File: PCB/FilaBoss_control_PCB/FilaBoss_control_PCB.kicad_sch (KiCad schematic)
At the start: 3 parts, among them J1 Screw_Terminal_01x02

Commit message: pcb
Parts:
- removed C1: C, symbol Device:C
- added C2: C, symbol Device:C
- added F1: Fuse, symbol Device:Fuse
- added J2, J4: Screw_Terminal_01x02, symbol Connector:Screw_Terminal_01x02
- added J3: Screw_Terminal_01x04, symbol Connector:Screw_Terminal_01x04
- added J5: Barrel_Jack_PTH_Slot, PCM_SparkFun-Connector:Barrel_Jack_PTH_Slot, symbol PCM_SparkFun-Connector:Barrel_Jack_PTH_Slot
- added M1, M2: Motor_DC, symbol Motor:Motor_DC
- added Q1, Q2: Q_NMOS, Package_TO_SOT_THT:TO-220F-3_Vertical, symbol Device:Q_NMOS
- added R1, R4: 100R, Resistor_THT:R_Axial_DIN0411_L9.9mm_D3.6mm_P12.70mm_Horizontal, symbol Device:R
- added R2, R3: 10K, Resistor_THT:R_Axial_DIN0411_L9.9mm_D3.6mm_P12.70mm_Horizontal, symbol Device:R
- added U1: ESP32_C3_super_mini, custom:ESP32-super-mini, symbol custom:ESP32_C3_super_mini
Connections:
- net at L1.1: now also F1.2
- net at L1.2: now also C2.1
- new net: Q2.G, R1.1, R2.1
- new net: J4.2 (Pin_2), M1.2 (-), Q1.D
- new net: Q1.G, R3.1, R4.1
- new net: C2.2, J2.1 (Pin_1), J4.1 (Pin_1), M1.1 (+), M2.1 (+)
- new net: J2.2 (Pin_2), M2.2 (-), Q2.D
- new net +24V: F1.1
- new net GND: Q1.S, Q2.S, R2.2, R3.2, U1.12 (GND)
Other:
- moved on the sheet: L1

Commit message: pcb v1 ready
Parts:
- removed J1, J4: Screw_Terminal_01x02, symbol Connector:Screw_Terminal_01x02
- removed J3: Screw_Terminal_01x04, symbol Connector:Screw_Terminal_01x04
- removed Q1: Q_NMOS, Package_TO_SOT_THT:TO-220F-3_Vertical, symbol Device:Q_NMOS
- added A1: Pololu_Breakout_A4988, Module:Pololu_Breakout-16_15.2x20.3mm, symbol Driver_Motor:Pololu_Breakout_A4988
- added C1, C3: C, Capacitor_THT:C_Axial_L5.1mm_D3.1mm_P10.00mm_Horizontal, symbol Device:C
- added D1, D2: D, Diode_THT:D_A-405_P10.16mm_Horizontal, symbol Device:D
- added J1, J9: Conn_01x04_Encoder, PCM_SparkFun-Connector:JST_1x04_P2.0mm_Vertical_PTH, symbol PCM_SparkFun-Connector:Conn_01x04_JST_P2.0mm_Vertical_PTH
- added J3: Screw_Terminal_01x02, TerminalBlock:TerminalBlock_Xinya_XY308-2.54-2P_1x02_P2.54mm_Horizontal, symbol Connector:Screw_Terminal_01x02
- added J6: PinHeader_01x06_P2.54mm_Vertical_THT_D1mm, PCM_fab:PinHeader_01x06_P2.54mm_Vertical_THT_D1mm, symbol PCM_fab:PinHeader_01x06_P2.54mm_Vertical_THT_D1mm
- added J7: Conn_01x04, PCM_SparkFun-Connector:JST_1x04_P2.0mm_Vertical_PTH, symbol PCM_SparkFun-Connector:Conn_01x04_JST_P2.0mm_Vertical_PTH
- added J8: JST_2mm_3, PCM_SparkFun-Connector:JST_1x03_P2.0mm_Vertical_PTH, symbol PCM_SparkFun-Connector:Conn_01x03_JST_P2.0mm_Vertical_PTH
- added Q1: IRLZ44N, Package_TO_SOT_THT:TO-220-3_Vertical, symbol Transistor_FET:IRLZ44N
- added SW1: RotaryEncoder_Switch, symbol Device:RotaryEncoder_Switch
- added U2: LM78M05_TO220, Package_TO_SOT_THT:TO-220-3_Vertical, symbol Regulator_Linear:LM78M05_TO220
- C2: footprint (none) -> Capacitor_THT:C_Axial_L5.1mm_D3.1mm_P10.00mm_Horizontal
- F1: footprint (none) -> Fuse:Fuseholder_Clip-5x20mm_Keystone_3512P_Inline_P23.62x7.27mm_D1.02x2.41x1.02x1.57mm_Horizontal
- J2: footprint (none) -> TerminalBlock:TerminalBlock_Xinya_XY308-2.54-2P_1x02_P2.54mm_Horizontal
- L1: footprint (none) -> Inductor_THT_Wurth:L_Wurth_WE-HCFT-2012_LeadDiameter1.2mm; Current (none) -> 4.5A; PROD_ID (none) -> NDUC-17223
- Q2: value Q_NMOS -> IRLZ44N; footprint Package_TO_SOT_THT:TO-220F-3_Vertical -> Package_TO_SOT_THT:TO-220-3_Vertical; symbol Device:Q_NMOS -> Transistor_FET:IRLZ44N
- R1, R2, R3, R4: footprint Resistor_THT:R_Axial_DIN0411_L9.9mm_D3.6mm_P12.70mm_Horizontal -> Resistor_THT:R_Axial_DIN0207_L6.3mm_D2.5mm_P10.16mm_Horizontal
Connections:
- net +24V: now also C2.1, L1.2, M1.1 (+), A1.8 (VMOT), D2.1 (K), J3.2 (Pin_2), J6.6 (Pin_6), U2.1 (VI); no longer F1.1
- net GND: now also C2.2, J5.GND, Q2.3 (S), A1.1 (GND), A1.7 (GND), A1.9 (~{ENABLE}), C1.2, C3.2, J1.4 (Pin_4), J6.2 (Pin_2), J8.1, J9.4 (Pin_4), Q1.3 (S), SW1.C, SW1.S2, U2.2 (GND); no longer Q2.S
- net at R1.1, R2.1: now also Q2.1 (G); no longer Q2.G
- net at M1.2 (-): now also D2.2 (A), J3.1 (Pin_1), Q1.2 (D)
- net at R3.1, R4.1: now also Q1.1 (G)
- net VDC: now reaches F1.2, L1.1
- net LINE: now reaches J5.PWR
- net LINE: now also F1.1
- net at R4.2: now also U1.4 (D2/A2)
- net at R1.2: now also U1.5 (D3/A3)
- net at U1.0 (ADC1-0): now also A1.16 (DIR)
- net at U1.1 (ADC1-1): now also A1.15 (STEP)
- net at U1.10 (D10/MOSI): now also J9.3 (Pin_3), SW1.B
- net +3.3V: now reaches U1.11 (3V3)
- net +3.3V: now also A1.10 (MS1), A1.11 (MS2), A1.12 (MS3), A1.13 (~{RESET}), A1.14 (~{SLEEP}), A1.2 (VDD), J1.3 (Pin_3), J6.1 (Pin_1)
- net +5V: now reaches U1.13 (5V)
- net +5V: now also C1.1, C3.1, U2.3 (VO)
- net at U1.2 (D0/A0): now also J1.2 (Pin_2)
- net at U1.20 (D7/RX): now also J8.2
- net at U1.21 (D6/TX): now also J8.3
- net at U1.3 (D1/A1): now also J1.1 (Pin_1)
- net at U1.6 (D4/SDA): now also J6.4 (Pin_4)
- net at U1.7 (D5/SCL): now also J6.3 (Pin_3)
- net at U1.8 (D8/SCK): now also J9.1 (Pin_1), SW1.S1
- net at U1.9 (D9/MISO): now also J9.2 (Pin_2), SW1.A
- new net: D1.1 (K), J2.2 (Pin_2), J6.5 (Pin_5), M2.1 (+)
- new net: D1.2 (A), J2.1 (Pin_1), M2.2 (-), Q2.2 (D)
- new net: A1.3 (1B), J7.1 (Pin_1)
- new net: A1.4 (1A), J7.2 (Pin_2)
- new net: A1.5 (2A), J7.3 (Pin_3)
- new net: A1.6 (2B), J7.4 (Pin_4)
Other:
- moved on the sheet: C2, F1, J2, J5, L1, M2, R1, R2, U1

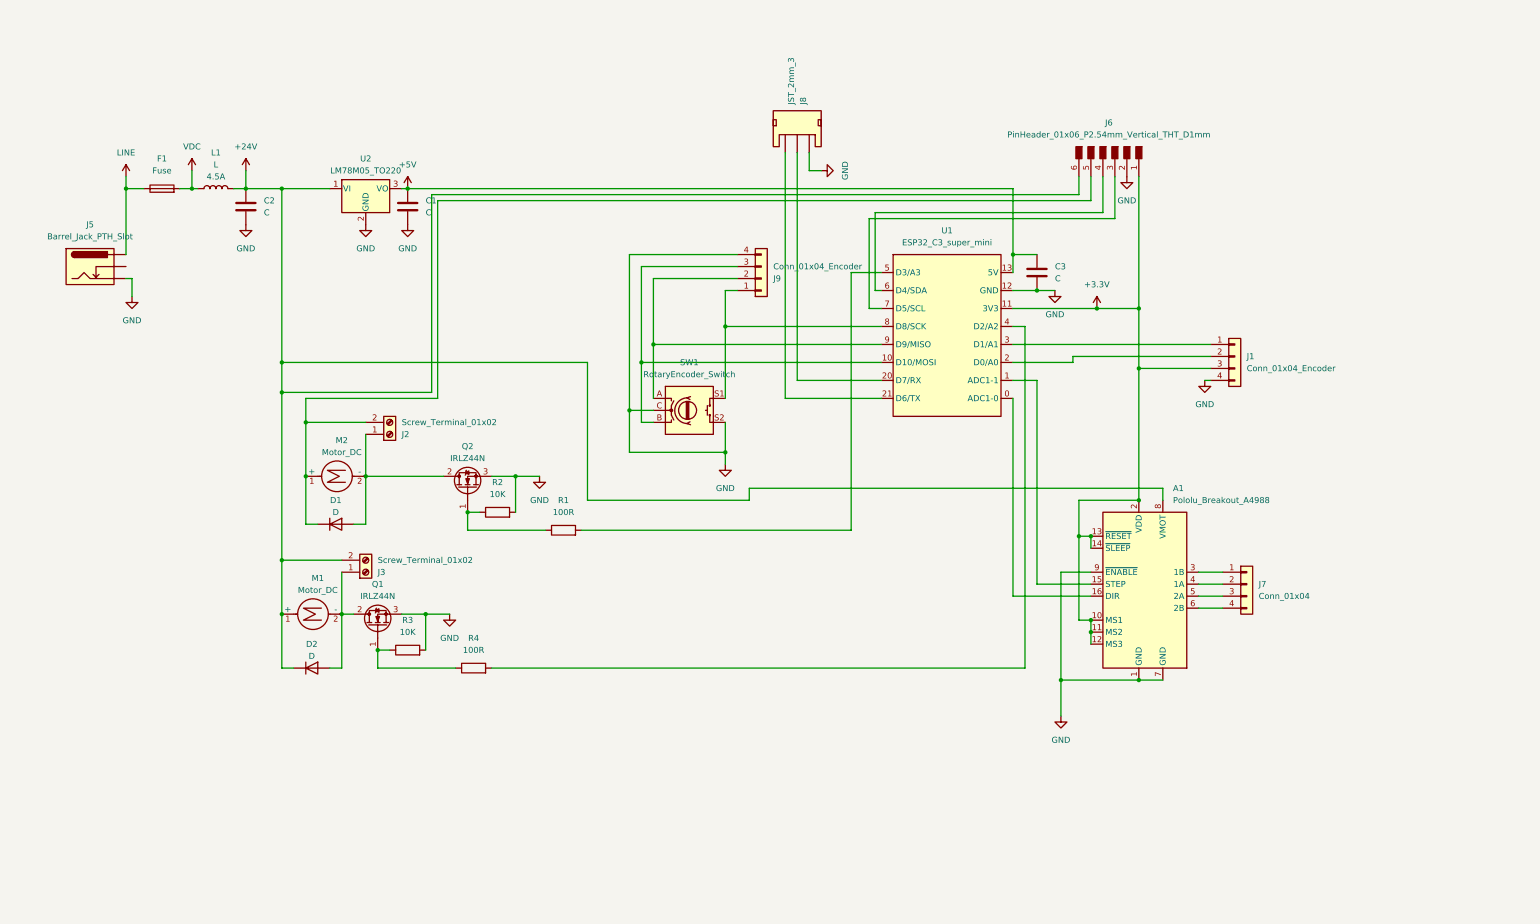
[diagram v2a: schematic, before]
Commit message: bigger esp required
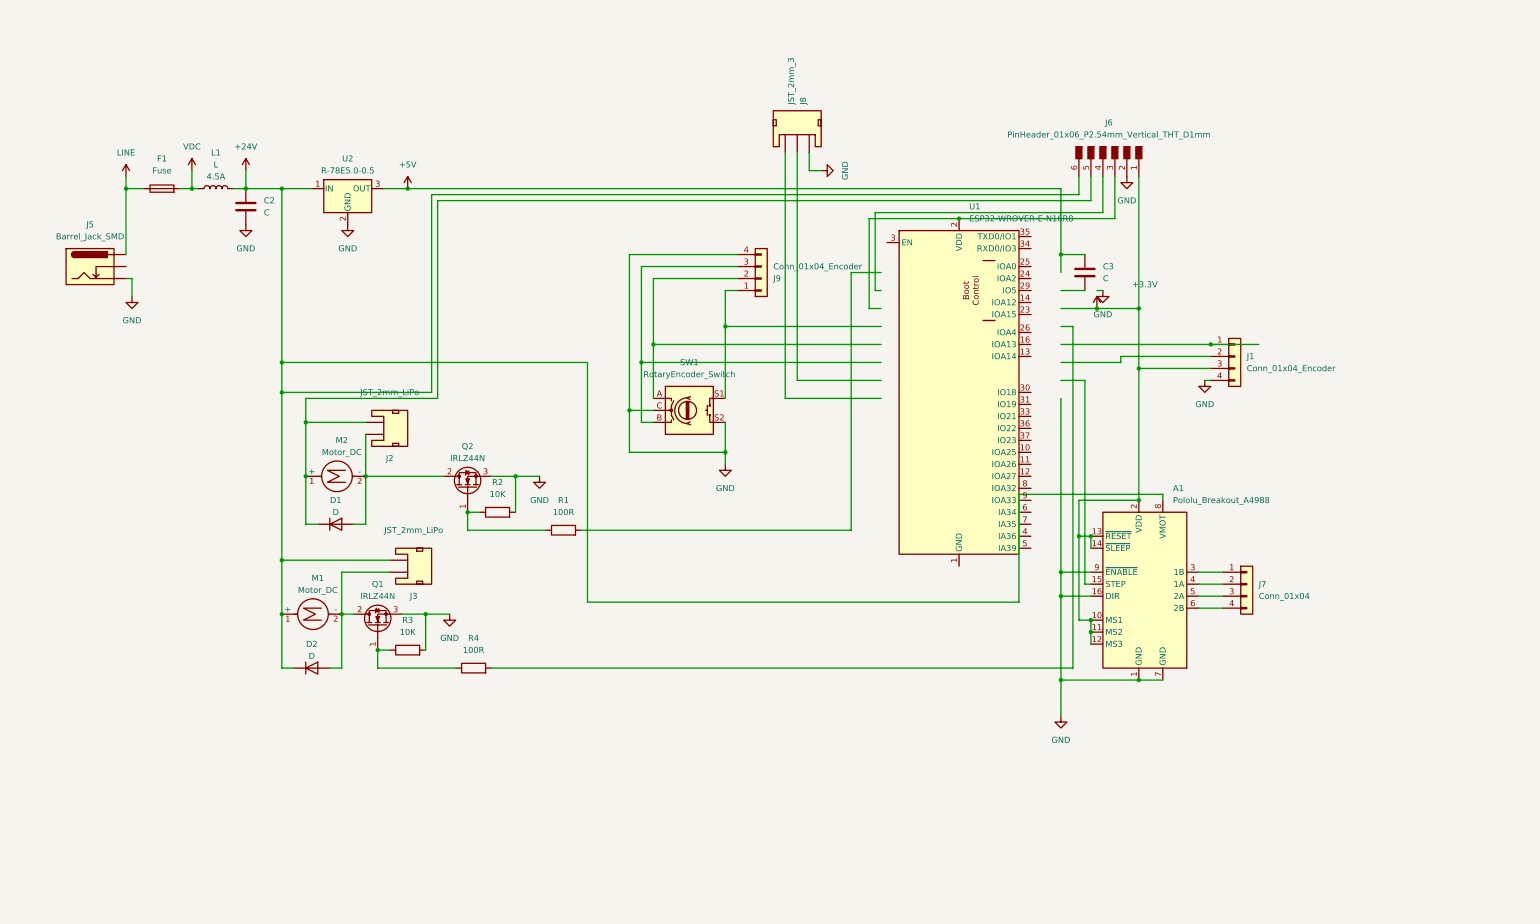
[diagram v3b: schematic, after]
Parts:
- removed C1: C, Capacitor_THT:C_Axial_L5.1mm_D3.1mm_P10.00mm_Horizontal, symbol Device:C
- removed J2, J3: Screw_Terminal_01x02, TerminalBlock:TerminalBlock_Xinya_XY308-2.54-2P_1x02_P2.54mm_Horizontal, symbol Connector:Screw_Terminal_01x02
- added J2, J3: JST_2mm_LiPo, Connector_JST:JST_PH_B2B-PH-K_1x02_P2.00mm_Vertical, symbol PCM_SparkFun-Connector:Conn_01x02_JST_P2.0mm_Horizontal_SMD
- F1: footprint Fuse:Fuseholder_Clip-5x20mm_Keystone_3512P_Inline_P23.62x7.27mm_D1.02x2.41x1.02x1.57mm_Horizontal -> Fuse:Fuseholder_Clip-5x20mm_Bel_FC-203-22_Lateral_P17.80x5.00mm_D1.17mm_Horizontal
- J5: value Barrel_Jack_PTH_Slot -> Barrel_Jack_SMD; footprint PCM_SparkFun-Connector:Barrel_Jack_PTH_Slot -> PCM_SparkFun-Connector:Barrel_Jack_SMD; symbol PCM_SparkFun-Connector:Barrel_Jack_PTH_Slot -> PCM_SparkFun-Connector:Barrel_Jack_SMD; PROD_ID CONN-08197 -> CONN-08106
- U1: value ESP32_C3_super_mini -> ESP32-WROVER-E-N16R8; footprint custom:ESP32-super-mini -> PCM_SparkFun-RF:ESP32-WROVER-E-IE; symbol custom:ESP32_C3_super_mini -> PCM_SparkFun-RF:ESP32-WROVER-E-N16R8; PROD_ID (none) -> IC-21314
- U2: value LM78M05_TO220 -> R-78E5.0-0.5; footprint Package_TO_SOT_THT:TO-220-3_Vertical -> Converter_DCDC:Converter_DCDC_RECOM_R-78E-0.5_THT; symbol Regulator_Linear:LM78M05_TO220 -> Converter_DCDC:R-78E5.0-0.5
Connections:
- net +24V: now also J3.1 (-)
- net +3.3V: no longer U1.11 (3V3)
- net +5V: no longer U1.13 (5V)
- net GND: now also A1.16 (DIR); no longer C3.2, U1.12 (GND)
- net at D2.2 (A), M1.2 (-), Q1.2 (D): now also J3.2 (+)
- net at D1.1 (K), J6.5 (Pin_5), M2.1 (+): now also J2.1 (-)
- net at D1.2 (A), M2.2 (-), Q2.2 (D): now also J2.2 (+)
- net at J9.1 (Pin_1), SW1.S1: no longer U1.8 (D8/SCK)
- net at J9.2 (Pin_2), SW1.A: no longer U1.9 (D9/MISO)
- net at J9.3 (Pin_3), SW1.B: no longer U1.10 (D10/MOSI)
- net at A1.15 (STEP): no longer U1.1 (ADC1-1)
- net at J1.1 (Pin_1): no longer U1.3 (D1/A1)
- net at J1.2 (Pin_2): no longer U1.2 (D0/A0)
- net at R4.2: no longer U1.4 (D2/A2)
- net at J6.3 (Pin_3): now also U1.2 (VDD); no longer U1.7 (D5/SCL)
- net at J6.4 (Pin_4): no longer U1.6 (D4/SDA)
- net at J8.2: no longer U1.20 (D7/RX)
- net at J8.3: no longer U1.21 (D6/TX)
- net at R1.2: no longer U1.5 (D3/A3)
- new net: U1.1 (GND), U1.15 (GND), U1.38 (GND), U1.39.1 (GND), U1.39.2 (GND), U1.39.3 (GND), U1.39.4 (GND), U1.39.5 (GND), U1.39.6 (GND), U1.39.7 (GND), U1.39.8 (GND), U1.39.9 (GND)
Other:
- moved on the sheet: C3, U2

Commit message: pcb converted to esp32 wroom
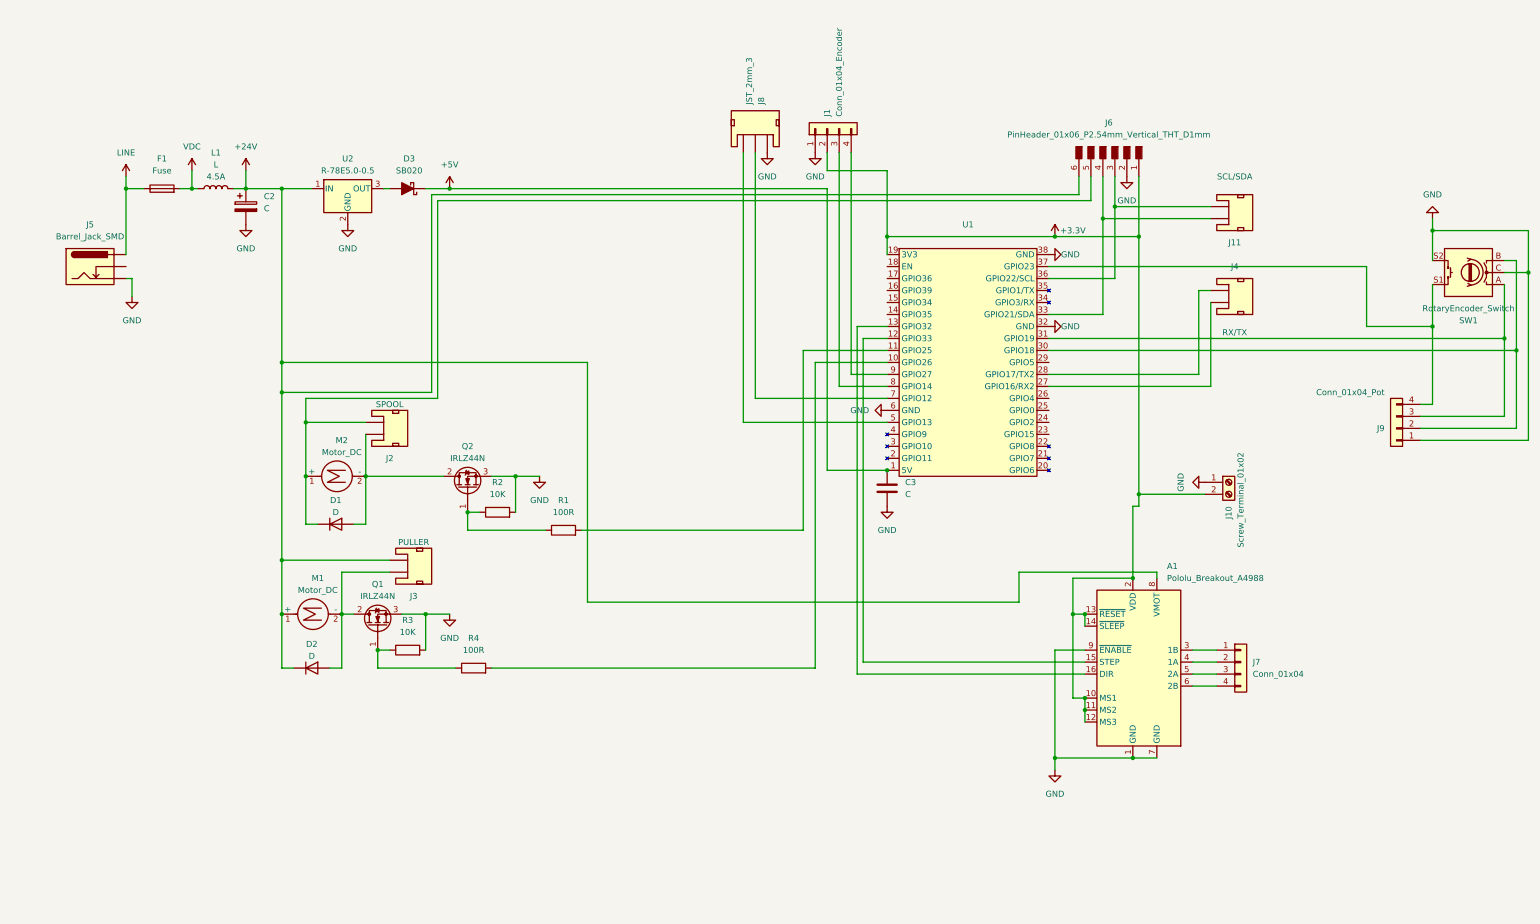
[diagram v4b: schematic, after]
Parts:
- removed U1: ESP32-WROVER-E-N16R8, PCM_SparkFun-RF:ESP32-WROVER-E-IE, symbol PCM_SparkFun-RF:ESP32-WROVER-E-N16R8
- added D3: SB020, PCM_Diode_THT_AKL:D_T-1_P7.62mm_Horizontal, symbol PCM_Diode_Schottky_AKL:SB020
- added J10: Screw_Terminal_01x02, TerminalBlock:TerminalBlock_Xinya_XY308-2.54-2P_1x02_P2.54mm_Horizontal, symbol Connector:Screw_Terminal_01x02
- added J11: SCL/SDA, Connector_JST:JST_PH_B2B-PH-K_1x02_P2.00mm_Vertical, symbol PCM_SparkFun-Connector:Conn_01x02_JST_P2.0mm_Horizontal_SMD
- added J4: RX/TX, Connector_JST:JST_PH_B2B-PH-K_1x02_P2.00mm_Vertical, symbol PCM_SparkFun-Connector:Conn_01x02_JST_P2.0mm_Horizontal_SMD
- added U1: ~, custom:ESP32 Wroom dev-kit, symbol custom:ESP_Wroom_32_dev_kit
- C2: footprint Capacitor_THT:C_Axial_L5.1mm_D3.1mm_P10.00mm_Horizontal -> Capacitor_THT:CP_Radial_D10.0mm_P5.00mm; symbol Device:C -> Device:C_Polarized
- J2: value JST_2mm_LiPo -> SPOOL
- J3: value JST_2mm_LiPo -> PULLER
- J9: value Conn_01x04_Encoder -> Conn_01x04_Pot
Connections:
- net +3.3V: now also J1.2 (Pin_2), J10.2 (Pin_2), U1.19 (3V3); no longer J1.3 (Pin_3)
- net +5V: now also C3.2, D3.1 (K), U1.1 (5V); no longer C3.1, U2.3 (OUT)
- net GND: now also C3.1, J1.1 (Pin_1), J9.1 (Pin_1), J10.1 (Pin_1), U1.32 (GND), U1.38 (GND), U1.6 (GND); no longer A1.16 (DIR), J1.4 (Pin_4), J9.4 (Pin_4)
- net at SW1.S1: now also J9.4 (Pin_4), U1.37 (GPIO23); no longer J9.1 (Pin_1)
- net at J9.2 (Pin_2): now also SW1.B, U1.30 (GPIO18); no longer SW1.A
- net at J9.3 (Pin_3): now also SW1.A, U1.31 (GPIO19); no longer SW1.B
- net at A1.15 (STEP): now also U1.12 (GPIO33)
- net at R4.2: now also U1.10 (GPIO26)
- net at J6.3 (Pin_3): now also J11.1 (-), U1.36 (GPIO22/SCL)
- net at J6.4 (Pin_4): now also J11.2 (+), U1.33 (GPIO21/SDA)
- net at J8.2: now also U1.7 (GPIO12)
- net at J8.3: now also U1.5 (GPIO13)
- net at R1.2: now also U1.11 (GPIO25)
- new net: D3.2 (A), U2.3 (OUT)
- new net: A1.16 (DIR), U1.13 (GPIO32)
- new net: J4.1 (-), U1.27 (GPIO16/RX2)
- new net: J4.2 (+), U1.28 (GPIO17/TX2)
- new net: J1.3 (Pin_3), U1.8 (GPIO14)
- new net: J1.4 (Pin_4), U1.9 (GPIO27)
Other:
- moved on the sheet: A1, C3, J1, J7, J8, J9, SW1

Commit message: pcb-schematic
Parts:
- added J12, J13: Screw_Terminal_01x02, TerminalBlock:TerminalBlock_Xinya_XY308-2.54-2P_1x02_P2.54mm_Horizontal, symbol Connector:Screw_Terminal_01x02
- added J14: Conn_01x04_Encoder, Connector_JST:JST_XA_B04B-XASK-1_1x04_P2.50mm_Vertical, symbol PCM_SparkFun-Connector:Conn_01x04_JST_P2.0mm_Vertical_PTH
- added U3: R-78B12-2.0, Converter_DCDC:Converter_DCDC_RECOM_R-78B-2.0_THT, symbol Converter_DCDC:R-78B12-2.0
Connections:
- net +24V: now also U3.1 (IN)
- net +5V: now also J13.1 (Pin_1)
- net GND: now also J12.2 (Pin_2), J13.2 (Pin_2), J14.1 (Pin_1), U3.2 (GND)
- net at U1.26 (GPIO4): now also J14.3 (Pin_3)
- net at U1.29 (GPIO5): now also J14.4 (Pin_4)
- new net +12V: J12.1 (Pin_1), J14.2 (Pin_2), U3.3 (OUT)

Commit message: pcb
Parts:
- added OC1: 4N35, PCM_Package_DIP_AKL:DIP-6_W7.62mm_LongPads, symbol PCM_Optocoupler_AKL:4N35
- F1: footprint Fuse:Fuseholder_Clip-5x20mm_Bel_FC-203-22_Lateral_P17.80x5.00mm_D1.17mm_Horizontal -> Fuse:Fuseholder_Clip-5x20mm_Littelfuse_521_Lateral_P17.00x5.00mm_D1.30mm_Horizontal
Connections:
- net +3.3V: no longer J1.2 (Pin_2)
- net +5V: now also J1.2 (Pin_2)
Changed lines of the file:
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@@
-	)
-	(junction
-		(at 198.12 46.99)
-		(diameter 0)
-		(color 0 0 0 0)
 	)
 	(junction
@@
 	)
 	(junction
+		(at 185.42 36.83)
+		(diameter 0)
+		(color 0 0 0 0)
+	)
+	(junction
 		(at 328.93 68.58)
 		(diameter 0)
@@
 	(wire
 		(pts
-			(xy 185.42 29.21) (xy 185.42 33.02)
-		)
-		(stroke
-			(width 0)
-			(type default)
-		)
-	)
-	(wire
-		(pts
 			(xy 140.97 30.48) (xy 140.97 36.83)
 		)
@@
 	(wire
 		(pts
+			(xy 185.42 29.21) (xy 185.42 36.83)
+		)
+		(stroke
+			(width 0)
+			(type default)
+		)
+	)
+	(wire
+		(pts
 			(xy 62.23 36.83) (xy 69.85 36.83)
 		)
@@
 	(wire
 		(pts
-			(xy 185.42 33.02) (xy 198.12 33.02)
-		)
-		(stroke
-			(width 0)
-			(type default)
-		)
-	)
-	(wire
-		(pts
 			(xy 82.55 127) (xy 85.09 127)
 		)
@@
 		(pts
 			(xy 250.19 157.48) (xy 233.68 157.48)
-		)
-		(stroke
-			(width 0)
-			(type default)
-		)
-	)
-	(wire
-		(pts
-			(xy 198.12 33.02) (xy 198.12 46.99)
 		)
 		(stroke
@@
 			)
 		)
-		(property "Footprint" "Fuse:Fuseholder_Clip-5x20mm_Bel_FC-203-22_Lateral_P17.80x5.00mm_D1.17mm_Horizontal"
+		(property "Footprint" "Fuse:Fuseholder_Clip-5x20mm_Littelfuse_521_Lateral_P17.00x5.00mm_D1.30mm_Horizontal"
 			(at 44.45 38.608 90)
 			(effects
@@
 					(unit 1)
 				)
+			)
+		)
+	)
+	(symbol
+		(lib_id "PCM_Optocoupler_AKL:4N35")
+		(at 158.75 99.06 0)
+		(unit 1)
+		(exclude_from_sim no)
+		(in_bom yes)
+		(on_board yes)
+		(dnp no)
+		(fields_autoplaced yes)
+		(property "Reference" "OC1"
+			(at 168.91 97.7899 0)
+			(effects
+				(font
+					(size 1.27 1.27)
+				)
+				(justify left)
+			)
+		)
+		(property "Value" "4N35"
+			(at 168.91 100.3299 0)
+			(effects
+				(font
+					(size 1.27 1.27)
+				)
+				(justify left)
+			)
+		)
+		(property "Footprint" "PCM_Package_DIP_AKL:DIP-6_W7.62mm_LongPads"
+			(at 153.67 106.68 0)
+			(effects
+				(font
+					(size 1.27 1.27)
+					(italic yes)
+				)
+				(justify left)
+				(hide yes)
+			)
+		)
+		(property "Datasheet" "https://www.tme.eu/Document/dcf7498395ab0bb3b43b93aa74a679d1/4N35-VIS.pdf"
+			(at 158.496 101.6 0)
+			(effects
+				(font
+					(size 1.27 1.27)
+				)
+				(justify left)
+				(hide yes)
+			)
+		)
+		(property "Description" "DIP-6 Optocoupler, Transistor output with base connection, 5kV, 10us, Alternate KiCAD Library"
+			(at 158.75 99.06 0)
+			(effects
+				(font
+					(size 1.27 1.27)
+				)
+				(hide yes)
+			)
+		)
+		(pin "3"
+		)
+		(pin "1"
+		)
+		(pin "6"
+		)
+		(pin "5"
+		)
+		(pin "4"
+		)
+		(pin "2"
+		)
+		(instances
+			(project ""
+				(path "/2f49582a-29fd-468d-b48c-a2b14259075d"
+					(reference "OC1")
+					(unit 1)
+				)
